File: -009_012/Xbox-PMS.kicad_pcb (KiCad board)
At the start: 4 copper layers, 151.7 x 39.8 mm, 142 parts, among them IC1 SIC437BED-T1-GE3, IC2 SIC437BED-T1-GE3, IC3 SIC437BED-T1-GE3, IC4 SIC437BED-T1-GE3, J2 USB_C_Receptacle_USB2.0_16P, J3 Jack-DC, J6 Conn_01x04_Pin, J7 Conn_01x04_Pin, J8 Conn_01x01_Pin, J9 Conn_01x01_Pin, U1 TVS2200DRV, U2 TPS25750, U3 CAT24C512

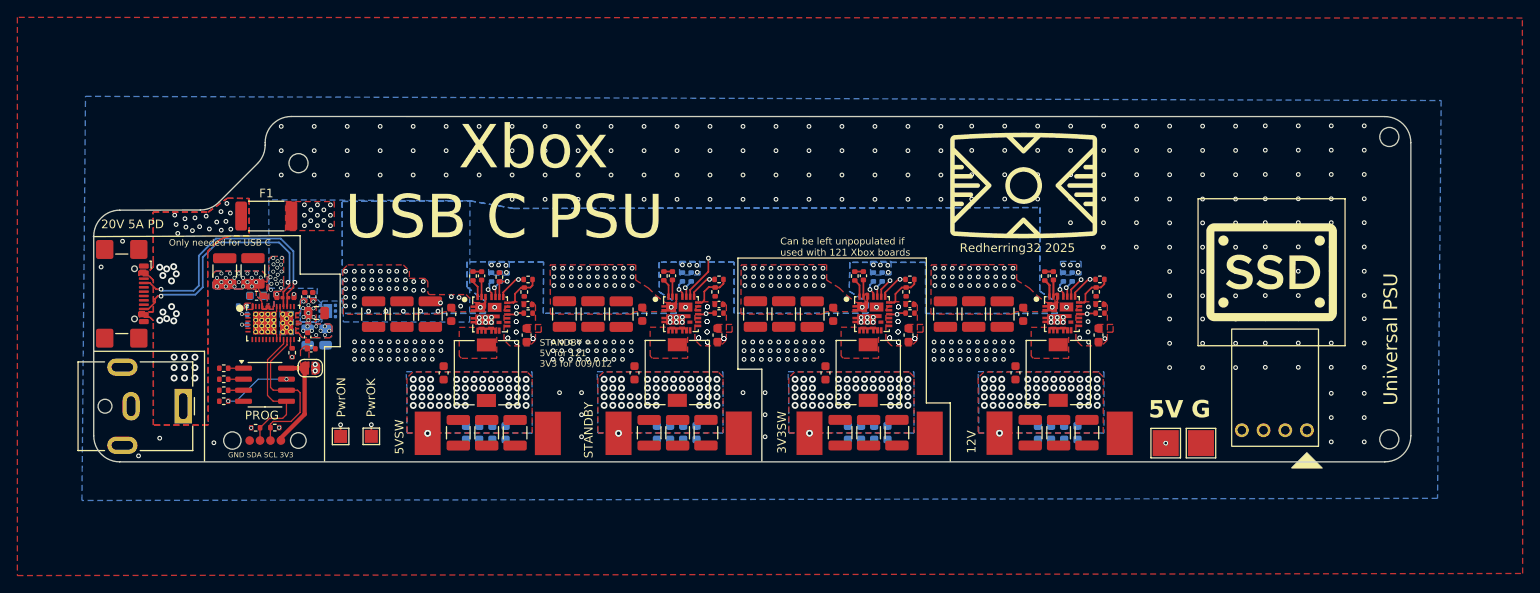
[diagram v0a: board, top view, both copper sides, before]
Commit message: Initial Changes
Updates for the following:

1.) Updated all inductor and capacitance values per equations in datasheet. Should minimize power supply ripple and minimize part cost.
2.) Added AND gate for power good output
3.) Rerouted board for simplicity and noise isolation.
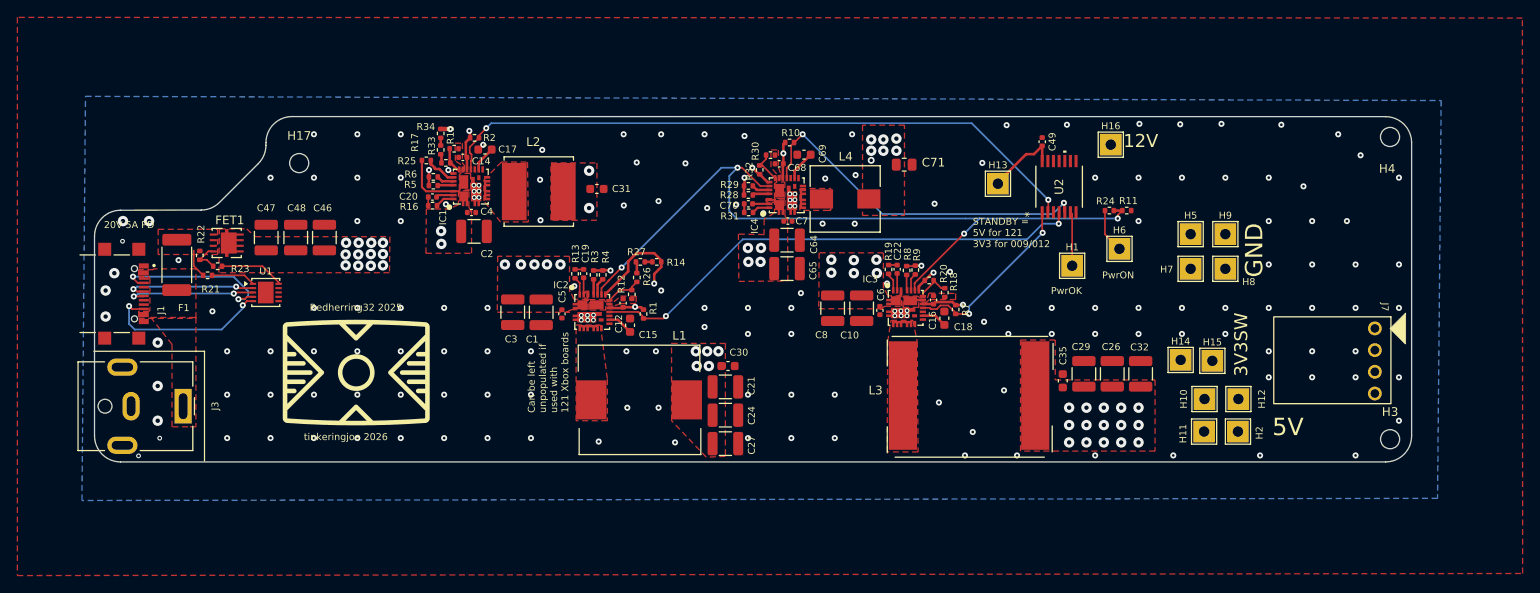
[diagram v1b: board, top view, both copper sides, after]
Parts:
- removed C11, C66: 22uF, Capacitor_SMD:C_1210_3225Metric
- removed C13, C33, C34, C36, C37, C38, C39, C40, C41, C44, C67, C74, C75, C76, C77, C9: 22uF, Capacitor_SMD:C_0603_1608Metric
- removed C23, C25, C28, C72, C73: 47uF, Capacitor_SMD:C_1210_3225Metric
- removed C42, C43, C45, C78: 0.1uF, Capacitor_SMD:C_0603_1608Metric
- removed C50, C52, C54, C61: 0.1uF 50V, Capacitor_SMD:C_0402_1005Metric
- removed C51, C53: 10uF 16V, Capacitor_SMD:C_0603_1608Metric
- removed C55, C56, C57: 10uF 16V, Capacitor_SMD:C_0402_1005Metric
- removed C58, C59: 22uF 50V, Capacitor_SMD:C_0805_2012Metric
- removed C60: 0.1uF, Capacitor_SMD:C_0402_1005Metric
- removed C62, C63: 330pF 16V, Capacitor_SMD:C_0201_0603Metric
- removed J2: USB_C_Receptacle_USB2.0_16P, Connector_USB:USB_C_Receptacle_GCT_USB4110
- removed J6: Conn_01x04_Pin, Xbox-Charge:PROG
- removed J8, J9: Conn_01x01_Pin, TestPoint:TestPoint_Pad_1.5x1.5mm
- removed JP1: Jumper_2_Open, Jumper:SolderJumper-2_P1.3mm_Open_RoundedPad1.0x1.5mm
- removed REF** (x3): MountingHole_2.2mm_M2, MountingHole:MountingHole_2.2mm_M2
- removed REF** (x2): TestPoint_Pad_3.0x3.0mm, TestPoint:TestPoint_Pad_3.0x3.0mm
- removed TP10, TP3, TP4, TP5, TP6, TP7, TP8, TP9: TestPoint, Xbox-PMS:pad
- removed U3: CAT24C512, Package_SO:SOIC-8_3.9x4.9mm_P1.27mm
- added FET1: AONR21307, Xbox-PMS:DFN8_3x3_EP_AOS, F.Cu at (45.0, 67.5)
- added H1: MountingHole_Pad, TestPoint:TestPoint_THTPad_2.5x2.5mm_Drill1.2mm, F.Cu at (142.3, 70.2)
- added H10: MountingHole_Pad, TestPoint:TestPoint_THTPad_2.5x2.5mm_Drill1.2mm, F.Cu at (157.6, 85.5)
- added H11: MountingHole_Pad, TestPoint:TestPoint_THTPad_2.5x2.5mm_Drill1.2mm, F.Cu at (157.6, 89.2)
- added H12: MountingHole_Pad, TestPoint:TestPoint_THTPad_2.5x2.5mm_Drill1.2mm, F.Cu at (161.5, 85.5)
- added H13: MountingHole_Pad, TestPoint:TestPoint_THTPad_2.5x2.5mm_Drill1.2mm, F.Cu at (133.8, 60.7)
- added H14: MountingHole_Pad, TestPoint:TestPoint_THTPad_2.5x2.5mm_Drill1.2mm, F.Cu at (154.8, 81.0)
- added H15: MountingHole_Pad, TestPoint:TestPoint_THTPad_2.5x2.5mm_Drill1.2mm, F.Cu at (158.5, 81.1)
- added H16: MountingHole_Pad, TestPoint:TestPoint_THTPad_2.5x2.5mm_Drill1.2mm, F.Cu at (146.8, 56.2)
- added H17: MountingHole, MountingHole:MountingHole_2.2mm_M2, F.Cu at (53.3, 58.3)
- added H2: MountingHole_Pad, TestPoint:TestPoint_THTPad_2.5x2.5mm_Drill1.2mm, F.Cu at (161.4, 89.2)
- added H3: MountingHole, MountingHole:MountingHole_2.2mm_M2, F.Cu at (179.0, 90.1)
- added H4: MountingHole, MountingHole:MountingHole_2.2mm_M2, F.Cu at (179.0, 55.3)
- added H5: MountingHole_Pad, TestPoint:TestPoint_THTPad_2.5x2.5mm_Drill1.2mm, F.Cu at (156.0, 66.5)
- added H6: MountingHole_Pad, TestPoint:TestPoint_THTPad_2.5x2.5mm_Drill1.2mm, F.Cu at (147.8, 68.2)
- added H7: MountingHole_Pad, TestPoint:TestPoint_THTPad_2.5x2.5mm_Drill1.2mm, F.Cu at (156.0, 70.5)
- added H8: MountingHole_Pad, TestPoint:TestPoint_THTPad_2.5x2.5mm_Drill1.2mm, F.Cu at (160.0, 70.5)
- added H9: MountingHole_Pad, TestPoint:TestPoint_THTPad_2.5x2.5mm_Drill1.2mm, F.Cu at (160.0, 66.5)
- added J1: GSB1C41110SSHR, Xbox-PMS:AMPHENOL_GSB1C41110SSHR, F.Cu at (31.7, 73.4)
- added R33: 15K, Resistor_SMD:R_0402_1005Metric, F.Cu at (69.6, 56.8)
- added R34: 15K, Resistor_SMD:R_0402_1005Metric, F.Cu at (69.6, 54.9)
- C12, C14, C16, C68: value 1uF -> 0.1uF
- C2: value 22uF -> 10uF
- C30, C31, C35, R28, R29, R3, R4, R5, R6, R8, R9: moved to F.Cu
- C4, C5, C6: value 22uF -> 0.1uF; footprint Capacitor_SMD:C_1210_3225Metric -> Capacitor_SMD:C_0402_1005Metric
- C46: value 100uF 16V -> 4.7u
- C47: value 4.7uF 50V -> 4.7u; footprint Capacitor_SMD:C_0805_2012Metric -> Capacitor_SMD:C_1210_3225Metric
- C48: value 0.1uF 50V -> 4.7u; footprint Capacitor_SMD:C_0402_1005Metric -> Capacitor_SMD:C_1210_3225Metric
- C49: value 100uF 16V -> 0.1uF; footprint Capacitor_SMD:C_1210_3225Metric -> Capacitor_SMD:C_0402_1005Metric
- C7: value 22uF -> 0.1uF; footprint Capacitor_SMD:C_0603_1608Metric -> Capacitor_SMD:C_0402_1005Metric
- C71: value 47uF -> 22uF; footprint Capacitor_SMD:C_1210_3225Metric -> Resistor_SMD:R_0805_2012Metric
- L1: value 780nH -> 26uH; footprint Inductor_SMD:L_7.3x7.3_H4.5 -> Xbox-PMS:fch1350-270M
- L2: value 820nH -> 330uH; footprint Inductor_SMD:L_7.3x7.3_H4.5 -> Xbox-PMS:IND_SRN8040TA-331M
- L3: value 780nH -> 10uH; footprint Inductor_SMD:L_7.3x7.3_H4.5 -> Xbox-PMS:MDA1870-100M
- L4: value 820nH -> 42uH; footprint Inductor_SMD:L_7.3x7.3_H4.5 -> Xbox-PMS:IND_ETQ-P4M470KFM_PAN
- R14, R17: value 45K -> 15K
- R15: value 2.55K -> 10K
- R21: value 10K -> 10
- R22: value 2.2K -> 49.9K
- R23: value 2.2K -> 5.1K
- R24, R25: value 10K -> 100K
- R26, R27: value 10K -> 15K
- R30: value 10K -> 430R
- R32: value 190K -> 8.2K
- U1: value TVS2200DRV -> HUSB238_xxxDD; footprint Package_SON:WSON-6-1EP_2x2mm_P0.65mm_EP1x1.6mm -> Package_DFN_QFN:WDFN-10-1EP_3x3mm_P0.5mm_EP1.8x2.5mm; moved to F.Cu
- U2: value TPS25750 -> 74VHC21FT; footprint Xbox-Charge:TPS25750D -> Xbox-PMS:TSSOP14B_TOS
- moved R24 103.6 mm to (146.6, 63.8), turned to 0 degrees
- moved C49 92.1 mm to (138.9, 55.9), turned to -90 degrees
- moved U2 91.9 mm to (140.8, 61.0), turned to 90 degrees
- moved C32 78.9 mm to (150.2, 82.6), turned to 90 degrees
- moved R11 72.7 mm to (148.6, 63.8), turned to 0 degrees
- moved C26 72.4 mm to (147.0, 82.6), turned to -90 degrees
- moved C35 67.5 mm to (141.3, 83.4), turned to 90 degrees
- moved C29 65.9 mm to (143.7, 82.6), turned to 90 degrees
- moved L3 53.0 mm to (127.8, 85.1), turned to 180 degrees
- moved C8 52.9 mm to (114.8, 75.0)
- moved R27 50.6 mm to (92.6, 69.7)
- moved C10 49.7 mm to (118.1, 75.0)
- moved R26 49.3 mm to (92.2, 71.5), turned to -90 degrees
- moved R7 49.2 mm to (128.9, 75.2), turned to 90 degrees
- moved R18 48.4 mm to (127.7, 73.2)
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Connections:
- C12 pad 2: /VDD -> /VDD_3V
- C14 pad 2: /VDD -> /VDD_3SB
- C15 pad 2: /VDD -> Net-(IC2-V_DRV)
- C16 pad 2: /VDD -> /VDD_5V
- C17 pad 2: /VDD -> Net-(IC1-V_DRV)
- C18 pad 2: /VDD -> Net-(IC3-V_DRV)
- C4 pad 1: /VBUS-SAFE -> GND
- C4 pad 2: GND -> /VBUS-SAFE
- C46 pad 1: /PP5V -> /VBUS-SAFE
- C49 pad 1: /PP5V -> GND
- C49 pad 2: GND -> /3V3SB
- C5 pad 1: /VBUS-SAFE -> GND
- C5 pad 2: GND -> /VBUS-SAFE
- C6 pad 1: /VBUS-SAFE -> GND
- C6 pad 2: GND -> /VBUS-SAFE
- C68 pad 2: /VDD -> /VDD_12V
- C69 pad 2: /VDD -> Net-(IC4-V_DRV)
- C7 pad 1: /VBUS-SAFE -> GND
- C7 pad 2: GND -> /VBUS-SAFE
- F1 pad 2: /VBUS-SAFE -> /VBUS-FUSED
- IC1 pad 12: /VDD -> Net-(IC1-V_DRV)
- IC1 pad 14: /PGOOD -> /PGOOD_3V3SB
- IC1 pad 15: /VDD -> /VDD_3SB
- IC1 pad 19: /VBUS-SAFE -> Net-(IC1-EN)
- IC2 pad 12: /VDD -> Net-(IC2-V_DRV)
- IC2 pad 14: /PGOOD -> /PGOOD_3V3
- IC2 pad 15: /VDD -> /VDD_3V
- IC3 pad 12: /VDD -> Net-(IC3-V_DRV)
- IC3 pad 14: /PGOOD -> /PGOOD_5V
- IC3 pad 15: /VDD -> /VDD_5V
- IC4 pad 12: /VDD -> Net-(IC4-V_DRV)
- IC4 pad 14: /PGOOD -> /PGOOD_12V
- IC4 pad 15: /VDD -> /VDD_12V
- R1 pad 1: /PGOOD -> /PGOOD_3V3
- R1 pad 2: /VDD -> /VDD_3V
- R10 pad 1: /PGOOD -> /PGOOD_12V
- R10 pad 2: /VDD -> /VDD_12V
- R14 pad 2: Net-(IC2-FB) -> Net-(R14-Pad2)
- R17 pad 1: /3V3SB -> Net-(R17-Pad1)
- R2 pad 1: /PGOOD -> /PGOOD_3V3SB
- R2 pad 2: /VDD -> /VDD_3SB
- R21 pad 1: /~{IRQ} -> /VBUS-FUSED
- R21 pad 2: /LDO_3V3 -> Net-(U1-VIN)
- R22 pad 1: /SDA -> /VBUS-FUSED
- R22 pad 2: /LDO_3V3 -> Net-(FET1-G)
- R23 pad 1: /SCL -> Net-(FET1-G)
- R23 pad 2: /LDO_3V3 -> Net-(U1-GATE)
- R24 pad 1: Net-(U3-A0) -> /ENABLE
- R24 pad 2: GND -> /EN
- R25 pad 1: Net-(U3-A1) -> /VBUS-SAFE
- R25 pad 2: GND -> Net-(IC1-EN)
- R26 pad 1: Net-(U3-A2) -> Net-(R26-Pad1)
- R26 pad 2: GND -> Net-(IC2-FB)
- R27 pad 1: Net-(U3-WP) -> Net-(R14-Pad2)
- R27 pad 2: GND -> Net-(R26-Pad1)
- R28 pad 2: /VDD -> /VDD_12V
- R29 pad 1: /VDD -> /VDD_12V
- R3 pad 2: /VDD -> /VDD_3V
- R4 pad 1: /VDD -> /VDD_3V
- R5 pad 2: /VDD -> /VDD_3SB
- R6 pad 1: /VDD -> /VDD_3SB
- R7 pad 1: /PGOOD -> /PGOOD_5V
- R7 pad 2: /VDD -> /VDD_5V
- R8 pad 2: /VDD -> /VDD_5V
- R9 pad 1: /VDD -> /VDD_5V
- U1 pad 1: GND -> Net-(U1-VIN)
- U1 pad 2: GND -> /D+
- U1 pad 3: GND -> /D-
- U1 pad 4: /VBUS-SAFE -> /CCx+
- U1 pad 5: /VBUS-SAFE -> /CCx-
- U1 pad 6: /VBUS-SAFE -> unconnected-(U1-SDA-Pad6)
- U1 pad 7: GND -> unconnected-(U1-SCL-Pad7)
- U2 pad 1: /LDO_3V3 -> /PGOOD_5V
- U2 pad 10: GND -> unconnected-(U2-Pad10)
- U2 pad 11: GND -> unconnected-(U2-Pad11)
- U2 pad 12: GND -> unconnected-(U2-Pad12)
- U2 pad 14: GND -> /3V3SB
- U2 pad 2: unconnected-(U2-ADCIN1-Pad2) -> /PGOOD_3V3SB
- U2 pad 4: /LDO_1V5 -> /PGOOD_3V3
- U2 pad 5: unconnected-(U2-GPIO0-Pad5) -> /PGOOD_12V
- U2 pad 6: unconnected-(U2-GPIO1-Pad6) -> /PGOOD
- U2 pad 7: unconnected-(U2-GPIO2-Pad7) -> GND
- U2 pad 8: GND -> unconnected-(U2-Pad8)
- U2 pad 9: GND -> unconnected-(U2-Pad9)
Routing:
- net /PGOOD: track 119.5 -> 6.24 mm, vias 5 -> 0
- net /PGOOD_3V3SB: track 0.00 -> 75.8 mm, vias 0 -> 2
- net /PGOOD_3V3: track 0.00 -> 58.0 mm, vias 0 -> 2
- net /3V3SB: track 39.4 -> 82.0 mm, vias 46 -> 4
- net /PGOOD_12V: track 0.00 -> 41.4 mm, vias 0 -> 2
- net /EN: track 126.5 -> 90.8 mm
- net /LDO_3V3: track 27.9 -> 0.00 mm, vias 6 -> 0
- net /PGOOD_5V: track 0.00 -> 21.3 mm, vias 0 -> 2
- net /12V: track 39.2 -> 18.9 mm, vias 46 -> 8
- net /SCL: track 18.1 -> 0.00 mm
- net /SDA: track 16.4 -> 0.00 mm
- net /3V3SW: track 39.3 -> 23.0 mm, vias 46 -> 6
- net /D+: track 0.00 -> 15.3 mm, vias 0 -> 2
- net /VDD_5V: track 0.00 -> 15.2 mm, vias 0 -> 2
- net /D-: track 0.00 -> 15.1 mm, vias 0 -> 2
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- added copper zone on In2.Cu, net /3V3SB
- added copper zone on In2.Cu, net /3V3SW
- added copper zone on F.Cu, net /VBUS-FUSED
- removed copper zone on B.Cu, net /12V
- removed copper zone on F.Cu, net /3V3
- removed copper zone on B.Cu, net /3V3SB
- removed copper zone on B.Cu, net /3V3SW
- removed copper zone on B.Cu, net /5VSW
- removed copper zone on B.Cu, net /DRAIN
- removed copper zone on F.Cu, net /EEPROM_3V3
- removed copper zone on B.Cu, net /PP5V
- removed copper zone on F.Cu, net /PP5V
- removed copper zone on B.Cu, net /PPHV
- removed copper zone on F.Cu, net /PPHV
- removed copper zone on B.Cu, net /VBUS-IN
- removed copper zone on In1.Cu, net /VBUS-IN
- removed copper zone on In2.Cu, net /VBUS-IN
- removed copper zone on B.Cu, net /VBUS-SAFE
- removed copper zone on In1.Cu, net /VBUS-SAFE
- removed copper zone on B.Cu, net /VDD
- removed copper zone on F.Cu, net /VDD
- removed copper zone on In2.Cu, net /VDD
- removed copper zone on In2.Cu, net GND
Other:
- board text added: "GND"
- board text added: "tinkeringjoe 2026"
- board text removed: "5VSW"
- board text removed: "G"
- board text removed: "GND SDA SCL 3V3"
- board text removed: "Only needed for USB C"
- board text removed: "PROG"
- board text removed: "STANDBY"
- board text removed: "Universal PSU"
- board text removed: "Xbox USB C PSU"
- board text removed: "{ "ViaStitching": "0.2", "stitch_zone_0": { "HSpacing": "1", "VSpacing": "1", "Clearance": "0", "Randomize": false } }"
